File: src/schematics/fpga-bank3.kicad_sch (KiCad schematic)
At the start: 1 part

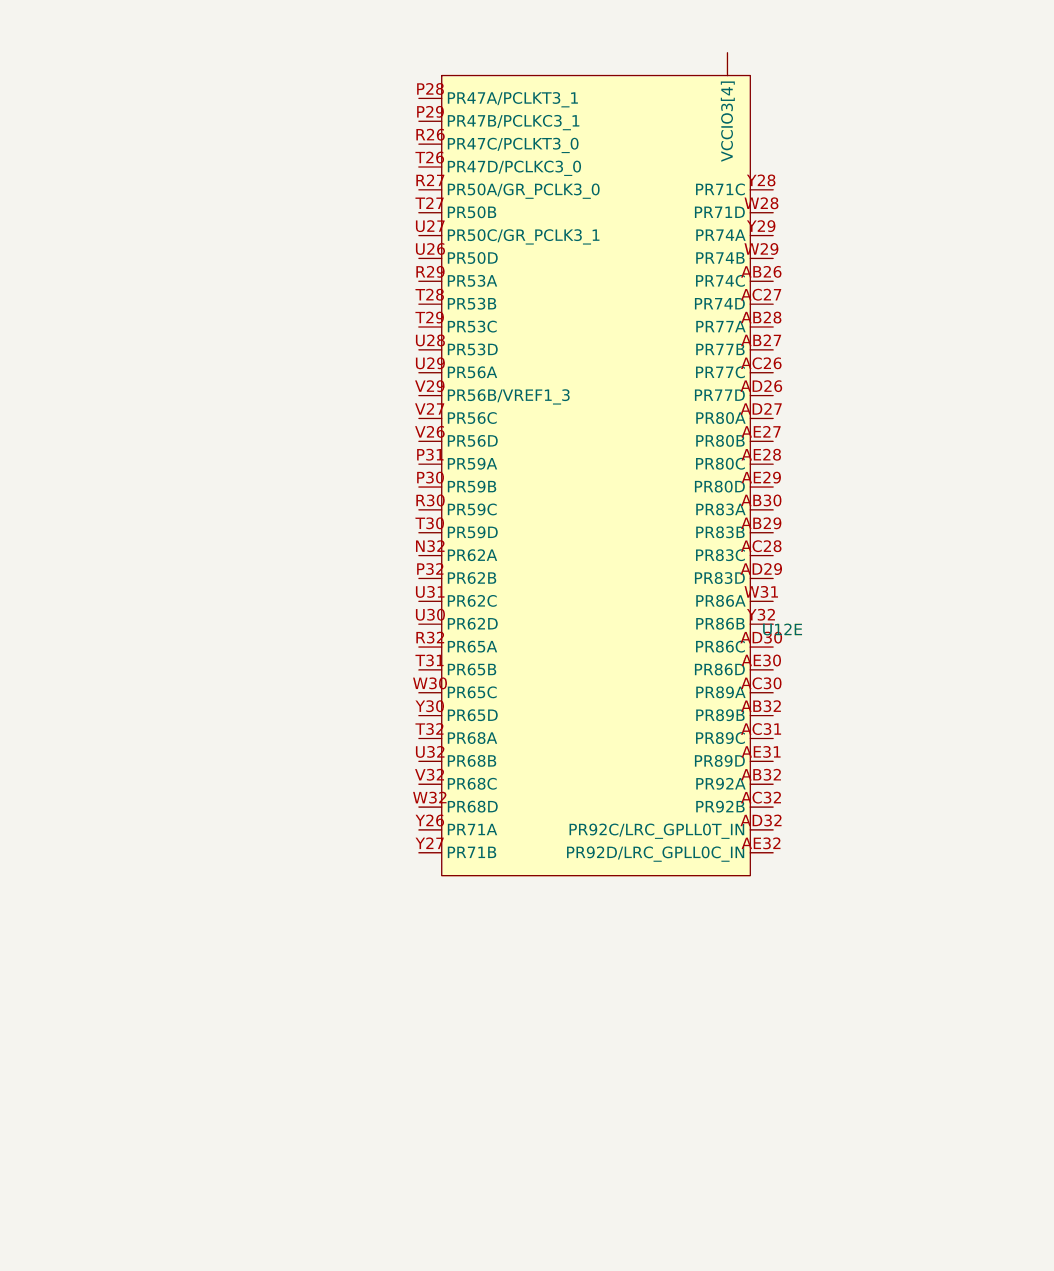
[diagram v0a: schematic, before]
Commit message: Draft connections between the FPGA and the memories
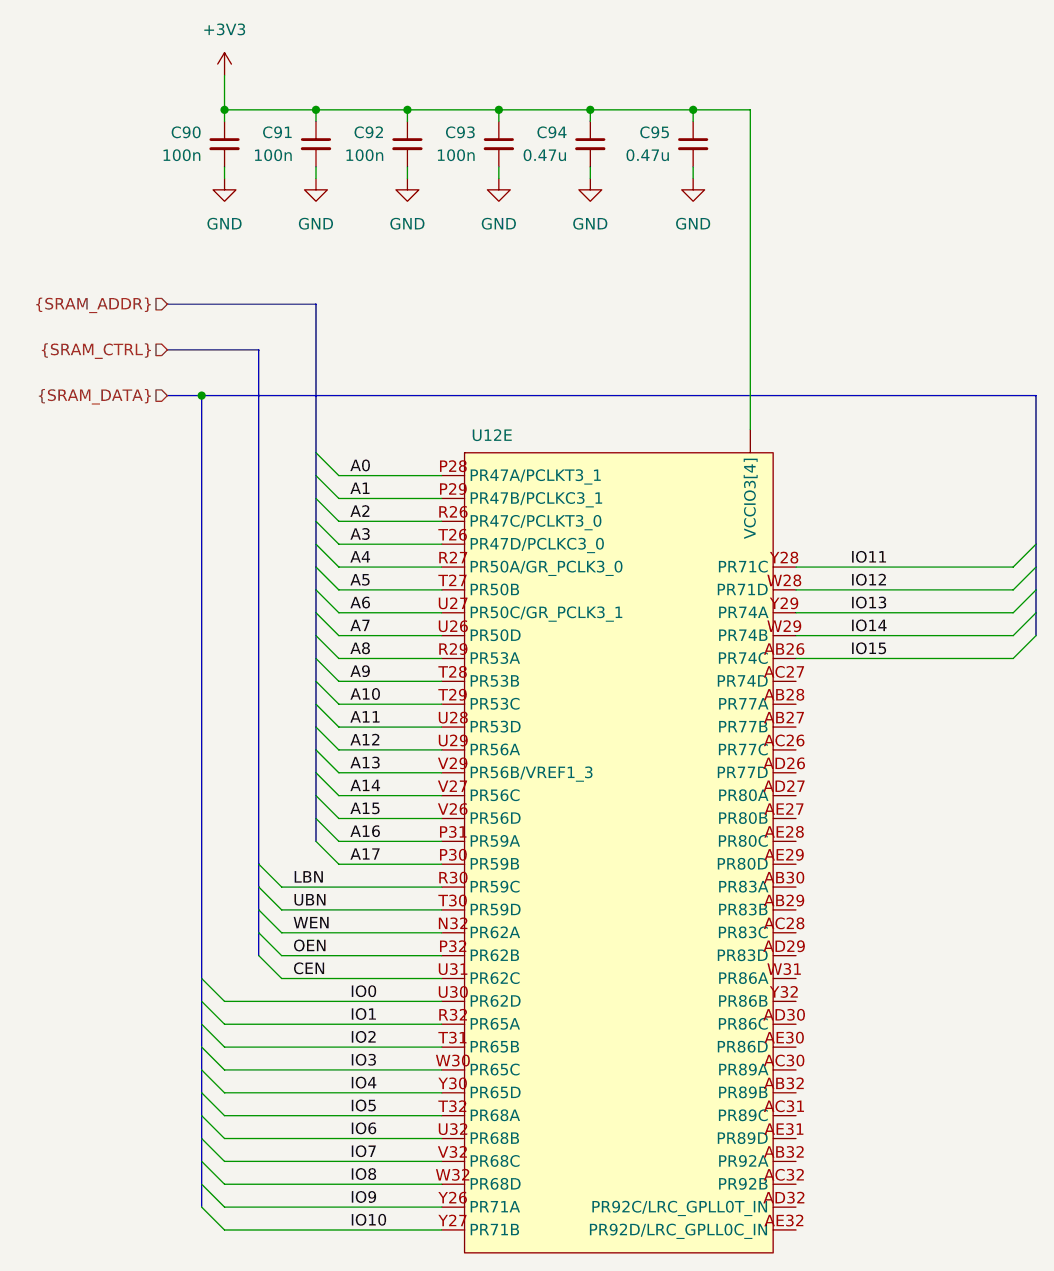
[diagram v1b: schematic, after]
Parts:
- added C90, C91, C92, C93: 100n, symbol Device:C_Small
- added C94, C95: 0.47u, symbol Device:C_Small
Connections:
- net IO15: now reaches U12.AB26 (PR74C)
- net WEN: now reaches U12.N32 (PR62A)
- net A0: now reaches U12.P28 (PR47A/PCLKT3_1)
- net A1: now reaches U12.P29 (PR47B/PCLKC3_1)
- net A17: now reaches U12.P30 (PR59B)
- net A16: now reaches U12.P31 (PR59A)
- net OEN: now reaches U12.P32 (PR62B)
- net A2: now reaches U12.R26 (PR47C/PCLKT3_0)
- net A4: now reaches U12.R27 (PR50A/GR_PCLK3_0)
- net A8: now reaches U12.R29 (PR53A)
- net LBN: now reaches U12.R30 (PR59C)
- net IO1: now reaches U12.R32 (PR65A)
- net A3: now reaches U12.T26 (PR47D/PCLKC3_0)
- net A5: now reaches U12.T27 (PR50B)
- net A9: now reaches U12.T28 (PR53B)
- net A10: now reaches U12.T29 (PR53C)
- net UBN: now reaches U12.T30 (PR59D)
- net IO2: now reaches U12.T31 (PR65B)
- net IO5: now reaches U12.T32 (PR68A)
- net A7: now reaches U12.U26 (PR50D)
- net A6: now reaches U12.U27 (PR50C/GR_PCLK3_1)
- net A11: now reaches U12.U28 (PR53D)
- net A12: now reaches U12.U29 (PR56A)
- net IO0: now reaches U12.U30 (PR62D)
- net CEN: now reaches U12.U31 (PR62C)
- net IO6: now reaches U12.U32 (PR68B)
- net A15: now reaches U12.V26 (PR56D)
- net A14: now reaches U12.V27 (PR56C)
- net A13: now reaches U12.V29 (PR56B/VREF1_3)
- net IO7: now reaches U12.V32 (PR68C)
- net IO12: now reaches U12.W28 (PR71D)
- net IO14: now reaches U12.W29 (PR74B)
- net IO3: now reaches U12.W30 (PR65C)
- net IO8: now reaches U12.W32 (PR68D)
- net IO9: now reaches U12.Y26 (PR71A)
- net IO10: now reaches U12.Y27 (PR71B)
- net IO11: now reaches U12.Y28 (PR71C)
- net IO13: now reaches U12.Y29 (PR74A)
- net IO4: now reaches U12.Y30 (PR65D)
- net VCCIO3 renamed +3V3
- net +3V3: now also C90.1, C91.1, C92.1, C93.1, C94.1, C95.1
- new net GND: C90.2, C91.2, C92.2, C93.2, C94.2, C95.2
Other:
- moved on the sheet: U12E

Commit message: Adds draft of IO connector schematic connections to FPGA
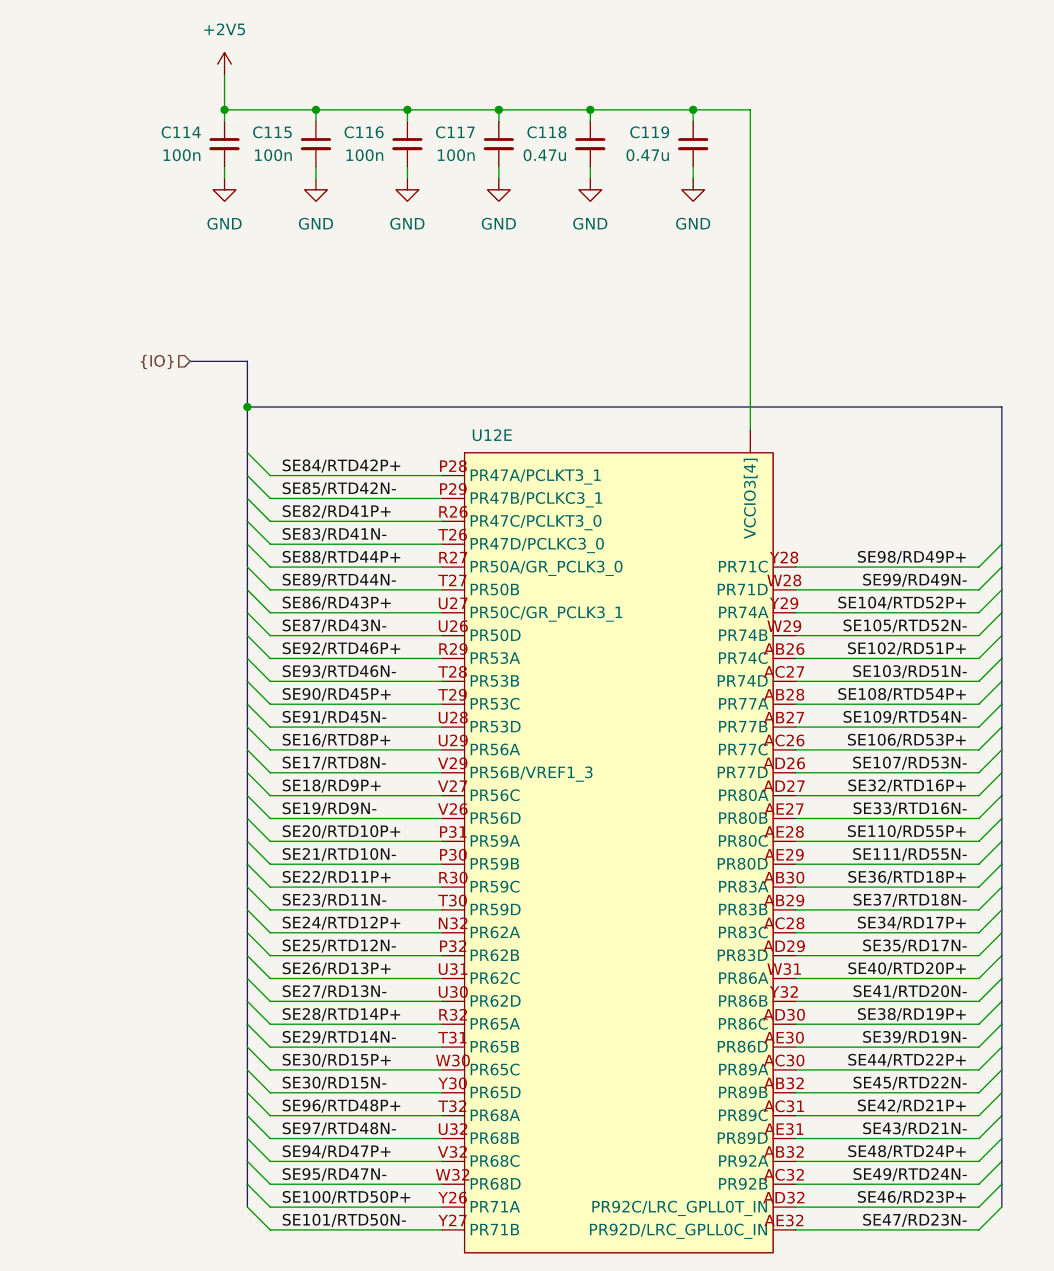
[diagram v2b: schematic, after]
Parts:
- removed C90, C91, C92, C93: 100n, symbol Device:C_Small
- removed C94, C95: 0.47u, symbol Device:C_Small
- added C114, C115, C116, C117: 100n, symbol Device:C_Small
- added C118, C119: 0.47u, symbol Device:C_Small
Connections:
- net GND: now also C114.2, C115.2, C116.2, C117.2, C118.2, C119.2
- net SE109/RTD54N-: now reaches U12.AB27 (PR77B)
- net SE108/RTD54P+: now reaches U12.AB28 (PR77A)
- net SE37/RTD18N-: now reaches U12.AB29 (PR83B)
- net SE36/RTD18P+: now reaches U12.AB30 (PR83A)
- net SE48/RTD24P+: now reaches U12.AB32 (PR92A)
- net SE106/RD53P+: now reaches U12.AC26 (PR77C)
- net SE103/RD51N-: now reaches U12.AC27 (PR74D)
- net SE34/RD17P+: now reaches U12.AC28 (PR83C)
- net SE44/RTD22P+: now reaches U12.AC30 (PR89A)
- net SE42/RD21P+: now reaches U12.AC31 (PR89C)
- net SE49/RTD24N-: now reaches U12.AC32 (PR92B)
- net SE107/RD53N-: now reaches U12.AD26 (PR77D)
- net SE32/RTD16P+: now reaches U12.AD27 (PR80A)
- net SE35/RD17N-: now reaches U12.AD29 (PR83D)
- net SE38/RD19P+: now reaches U12.AD30 (PR86C)
- net SE46/RD23P+: now reaches U12.AD32 (PR92C/LRC_GPLL0T_IN)
- net SE33/RTD16N-: now reaches U12.AE27 (PR80B)
- net SE110/RD55P+: now reaches U12.AE28 (PR80C)
- net SE111/RD55N-: now reaches U12.AE29 (PR80D)
- net SE39/RD19N-: now reaches U12.AE30 (PR86D)
- net SE43/RD21N-: now reaches U12.AE31 (PR89D)
- net SE47/RD23N-: now reaches U12.AE32 (PR92D/LRC_GPLL0C_IN)
- net SE40/RTD20P+: now reaches U12.W31 (PR86A)
- net SE41/RTD20N-: now reaches U12.Y32 (PR86B)
- net +3V3 renamed +2V5
- net +2V5: now also C114.1, C115.1, C116.1, C117.1, C118.1, C119.1
- net A0 renamed SE84/RTD42P+
- net A1 renamed SE85/RTD42N-
- net A10 renamed SE90/RD45P+
- net A11 renamed SE91/RD45N-
- net A12 renamed SE16/RTD8P+
- net A13 renamed SE17/RTD8N-
- net A14 renamed SE18/RD9P+
- net A15 renamed SE19/RD9N-
- net A16 renamed SE20/RTD10P+
- net A17 renamed SE21/RTD10N-
- net A2 renamed SE82/RD41P+
- net A3 renamed SE83/RD41N-
- net A4 renamed SE88/RTD44P+
- net A5 renamed SE89/RTD44N-
- net A6 renamed SE86/RD43P+
- net A7 renamed SE87/RD43N-
- net A8 renamed SE92/RTD46P+
- net A9 renamed SE93/RTD46N-
- net CEN renamed SE26/RD13P+
- net IO0 renamed SE27/RD13N-
- net IO1 renamed SE28/RTD14P+
- net IO10 renamed SE101/RTD50N-
- net IO11 renamed SE98/RD49P+
- net IO12 renamed SE99/RD49N-
- net IO13 renamed SE104/RTD52P+
- net IO14 renamed SE105/RTD52N-
- net IO15 renamed SE102/RD51P+
- net IO2 renamed SE29/RTD14N-
- net IO3 renamed SE30/RD15P+
- net IO4 renamed SE30/RD15N-
- net IO5 renamed SE96/RTD48P+
- net IO6 renamed SE97/RTD48N-
- net IO7 renamed SE94/RD47P+
- net IO8 renamed SE95/RD47N-
- net IO9 renamed SE100/RTD50P+
- net LBN renamed SE22/RD11P+
- net OEN renamed SE25/RTD12N-
- net UBN renamed SE23/RD11N-
- net WEN renamed SE24/RTD12P+
- new net SE45/RTD22N-: U12.AB32 (PR92A)

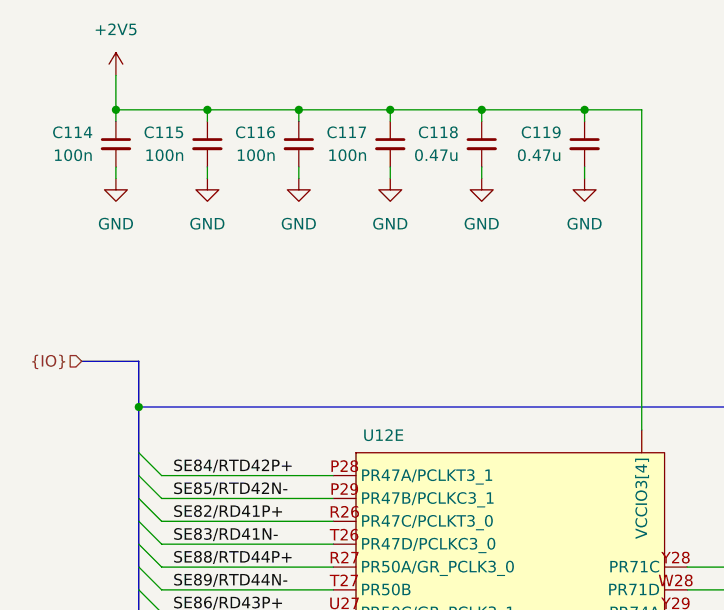
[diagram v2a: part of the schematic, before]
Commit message: Adds the clock oscillator
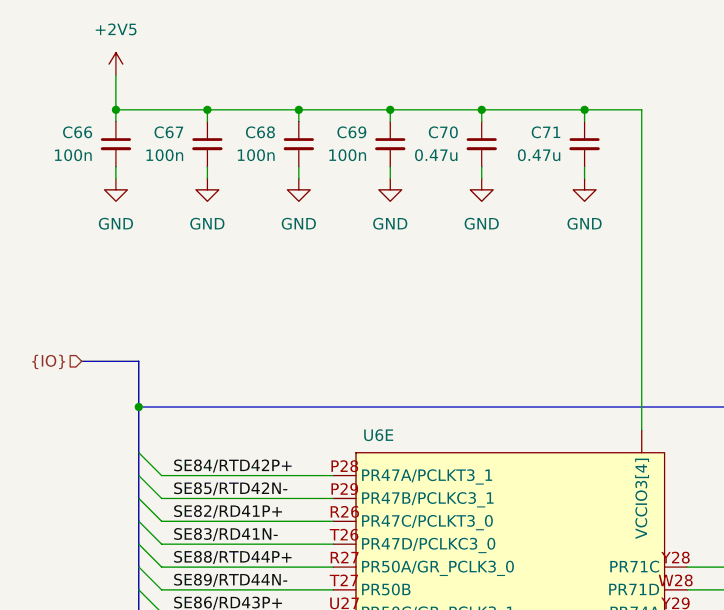
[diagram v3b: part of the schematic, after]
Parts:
- removed U12: ~, symbol ECAP5-BSOM:LFE5U-85F-*BG756*
- added U6: ~, symbol ECAP5-BSOM:LFE5U-85F-*BG756*
- renumbered C114 to C66, C115 to C67, C116 to C68, C117 to C69, C118 to C70, C119 to C71
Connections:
- net +2V5: now also U6. (VCCIO3[4]), U6.AA23 (VCCIO3), U6.U23 (VCCIO3), U6.V23 (VCCIO3), U6.W23 (VCCIO3)
- net SE100/RTD50P+: now also U6.Y26 (PR71A)
- net SE101/RTD50N-: now also U6.Y27 (PR71B)
- net SE102/RD51P+: now also U6.AB26 (PR74C)
- net SE103/RD51N-: now also U6.AC27 (PR74D)
- net SE104/RTD52P+: now also U6.Y29 (PR74A)
- net SE105/RTD52N-: now also U6.W29 (PR74B)
- net SE106/RD53P+: now also U6.AC26 (PR77C)
- net SE107/RD53N-: now also U6.AD26 (PR77D)
- net SE108/RTD54P+: now also U6.AB28 (PR77A)
- net SE109/RTD54N-: now also U6.AB27 (PR77B)
- net SE110/RD55P+: now also U6.AE28 (PR80C)
- net SE111/RD55N-: now also U6.AE29 (PR80D)
- net SE16/RTD8P+: now also U6.U29 (PR56A)
- net SE17/RTD8N-: now also U6.V29 (PR56B/VREF1_3)
- net SE18/RD9P+: now also U6.V27 (PR56C)
- net SE19/RD9N-: now also U6.V26 (PR56D)
- net SE20/RTD10P+: now also U6.P31 (PR59A)
- net SE21/RTD10N-: now also U6.P30 (PR59B)
- net SE22/RD11P+: now also U6.R30 (PR59C)
- net SE23/RD11N-: now also U6.T30 (PR59D)
- net SE24/RTD12P+: now also U6.N32 (PR62A)
- net SE25/RTD12N-: now also U6.P32 (PR62B)
- net SE26/RD13P+: now also U6.U31 (PR62C)
- net SE27/RD13N-: now also U6.U30 (PR62D)
- net SE28/RTD14P+: now also U6.R32 (PR65A)
- net SE29/RTD14N-: now also U6.T31 (PR65B)
- net SE30/RD15N-: now also U6.Y30 (PR65D)
- net SE30/RD15P+: now also U6.W30 (PR65C)
- net SE32/RTD16P+: now also U6.AD27 (PR80A)
- net SE33/RTD16N-: now also U6.AE27 (PR80B)
- net SE34/RD17P+: now also U6.AC28 (PR83C)
- net SE35/RD17N-: now also U6.AD29 (PR83D)
- net SE36/RTD18P+: now also U6.AB30 (PR83A)
- net SE37/RTD18N-: now also U6.AB29 (PR83B)
- net SE38/RD19P+: now also U6.AD30 (PR86C)
- net SE39/RD19N-: now also U6.AE30 (PR86D)
- net SE40/RTD20P+: now also U6.W31 (PR86A)
- net SE41/RTD20N-: now also U6.Y32 (PR86B)
- net SE42/RD21P+: now also U6.AC31 (PR89C)
- net SE43/RD21N-: now also U6.AE31 (PR89D)
- net SE44/RTD22P+: now also U6.AC30 (PR89A)
- net SE45/RTD22N-: now also U6.AB32 (PR92A)
- net SE46/RD23P+: now also U6.AD32 (PR92C/LRC_GPLL0T_IN)
- net SE47/RD23N-: now also U6.AE32 (PR92D/LRC_GPLL0C_IN)
- net SE48/RTD24P+: now also U6.AB32 (PR92A)
- net SE49/RTD24N-: now also U6.AC32 (PR92B)
- net SE82/RD41P+: now also U6.R26 (PR47C/PCLKT3_0)
- net SE83/RD41N-: now also U6.T26 (PR47D/PCLKC3_0)
- net SE84/RTD42P+: now also U6.P28 (PR47A/PCLKT3_1)
- net SE85/RTD42N-: now also U6.P29 (PR47B/PCLKC3_1)
- net SE86/RD43P+: now also U6.U27 (PR50C/GR_PCLK3_1)
- net SE87/RD43N-: now also U6.U26 (PR50D)
- net SE88/RTD44P+: now also U6.R27 (PR50A/GR_PCLK3_0)
- net SE89/RTD44N-: now also U6.T27 (PR50B)
- net SE90/RD45P+: now also U6.T29 (PR53C)
- net SE91/RD45N-: now also U6.U28 (PR53D)
- net SE92/RTD46P+: now also U6.R29 (PR53A)
- net SE93/RTD46N-: now also U6.T28 (PR53B)
- net SE94/RD47P+: now also U6.V32 (PR68C)
- net SE95/RD47N-: now also U6.W32 (PR68D)
- net SE96/RTD48P+: now also U6.T32 (PR68A)
- net SE97/RTD48N-: now also U6.U32 (PR68B)
- net SE98/RD49P+: now also U6.Y28 (PR71C)
- net SE99/RD49N-: now also U6.W28 (PR71D)

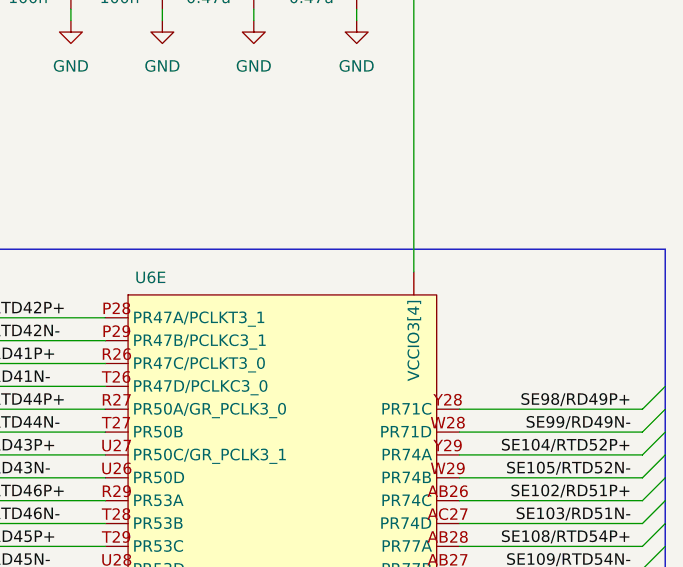
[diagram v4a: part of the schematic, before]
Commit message: Fix some ERC issues
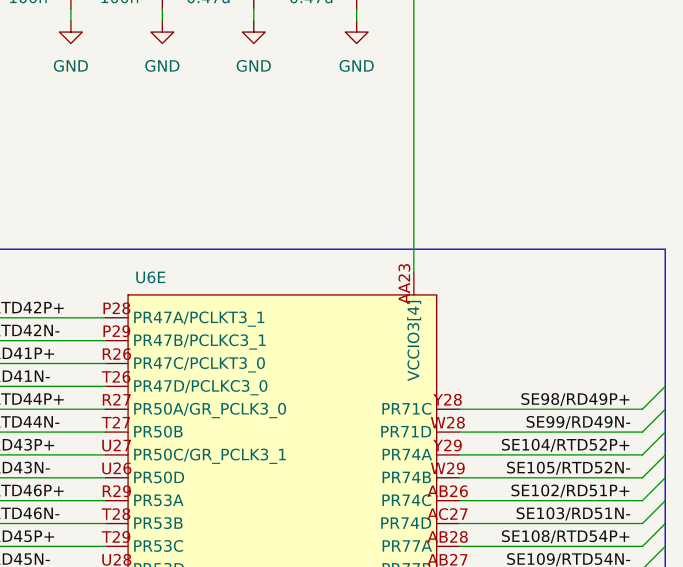
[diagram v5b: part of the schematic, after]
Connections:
- net +2V5: no longer U6. (VCCIO3[4])
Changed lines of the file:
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@@
 		(pin "Y31"
 		)
-		(pin ""
-		)
 		(pin "A10"
 		)
@@
 		(pin "Y32"
 		)
-		(pin ""
-		)
 		(pin "AB23"
 		)
@@
 		(pin "K16"
 		)
-		(pin ""
-		)
 		(pin "A18"
 		)
@@
 		(pin "K21"
 		)
-		(pin ""
-		)
 		(pin "B32"
 		)
@@
 		(pin "T23"
 		)
-		(pin ""
-		)
 		(pin "AA23"
 		)
@@
 		(pin "AM31"
 		)
-		(pin ""
-		)
 		(pin "AA10"
 		)
@@
 		(pin "Y7"
 		)
-		(pin ""
-		)
 		(pin "B1"
 		)
@@
 		(pin "T10"
 		)
-		(pin ""
-		)
 		(pin "AB10"
 		)
@@
 		(pin "M14"
 		)
-		(pin ""
-		)
 		(pin "AH12"
 		)
@@
 		(pin "V19"
 		)
-		(pin ""
-		)
 		(pin "AC11"
 		)
@@
 		(pin "AA11"
 		)
-		(pin ""
-		)
 		(instances

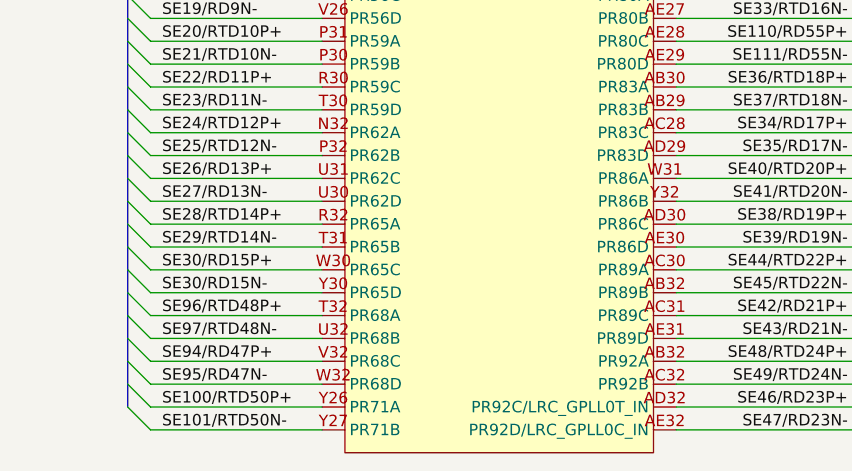
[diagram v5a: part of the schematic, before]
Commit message: Fixes bus aliases
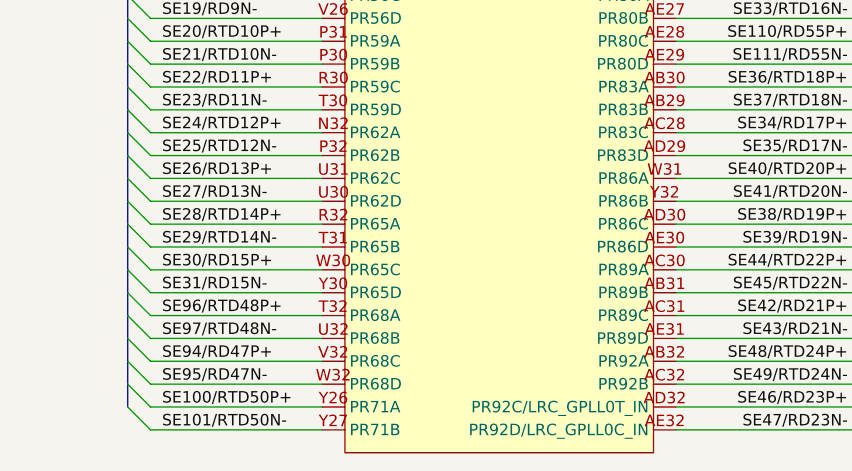
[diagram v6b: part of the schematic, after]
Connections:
- net SE45/RTD22N-: now also U6.AB31 (PR89B); no longer U6.AB32 (PR92A)
- net SE30/RD15N- renamed SE31/RD15N-
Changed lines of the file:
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@@
 		)
 	)
-	(label "SE30{slash}RD15N-"
+	(label "SE31{slash}RD15N-"
 		(at 119.38 144.78 0)
 		(fields_autoplaced yes)
@@
 		(pin "AB32"
 		)
-		(pin "AB32"
+		(pin "AB31"
 		)
 		(pin "AC26"
